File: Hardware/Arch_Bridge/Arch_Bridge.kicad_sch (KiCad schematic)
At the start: 94 parts, among them J1 Conn_01x02, J5V1 Conn_01x02, Q1 MMBT3904, Q2 MMBT3906, Q3 MJE2955, U1 AP63205WU, U11 ESP32-S3-WROOM-1, U12 TXS0102DCT, U13 DRV8231ADDAR, U17 TXS0102DCT, U18 TXS0102DCT, U19 TXS0108EPW, U2 TLV1117LV33DCYR, U20 TXS0108EPW, U3 LM393B, U4 74LVC1G04, U5 74LVC1G02, U6 TLP2770, U7 DRV8231ADDAR

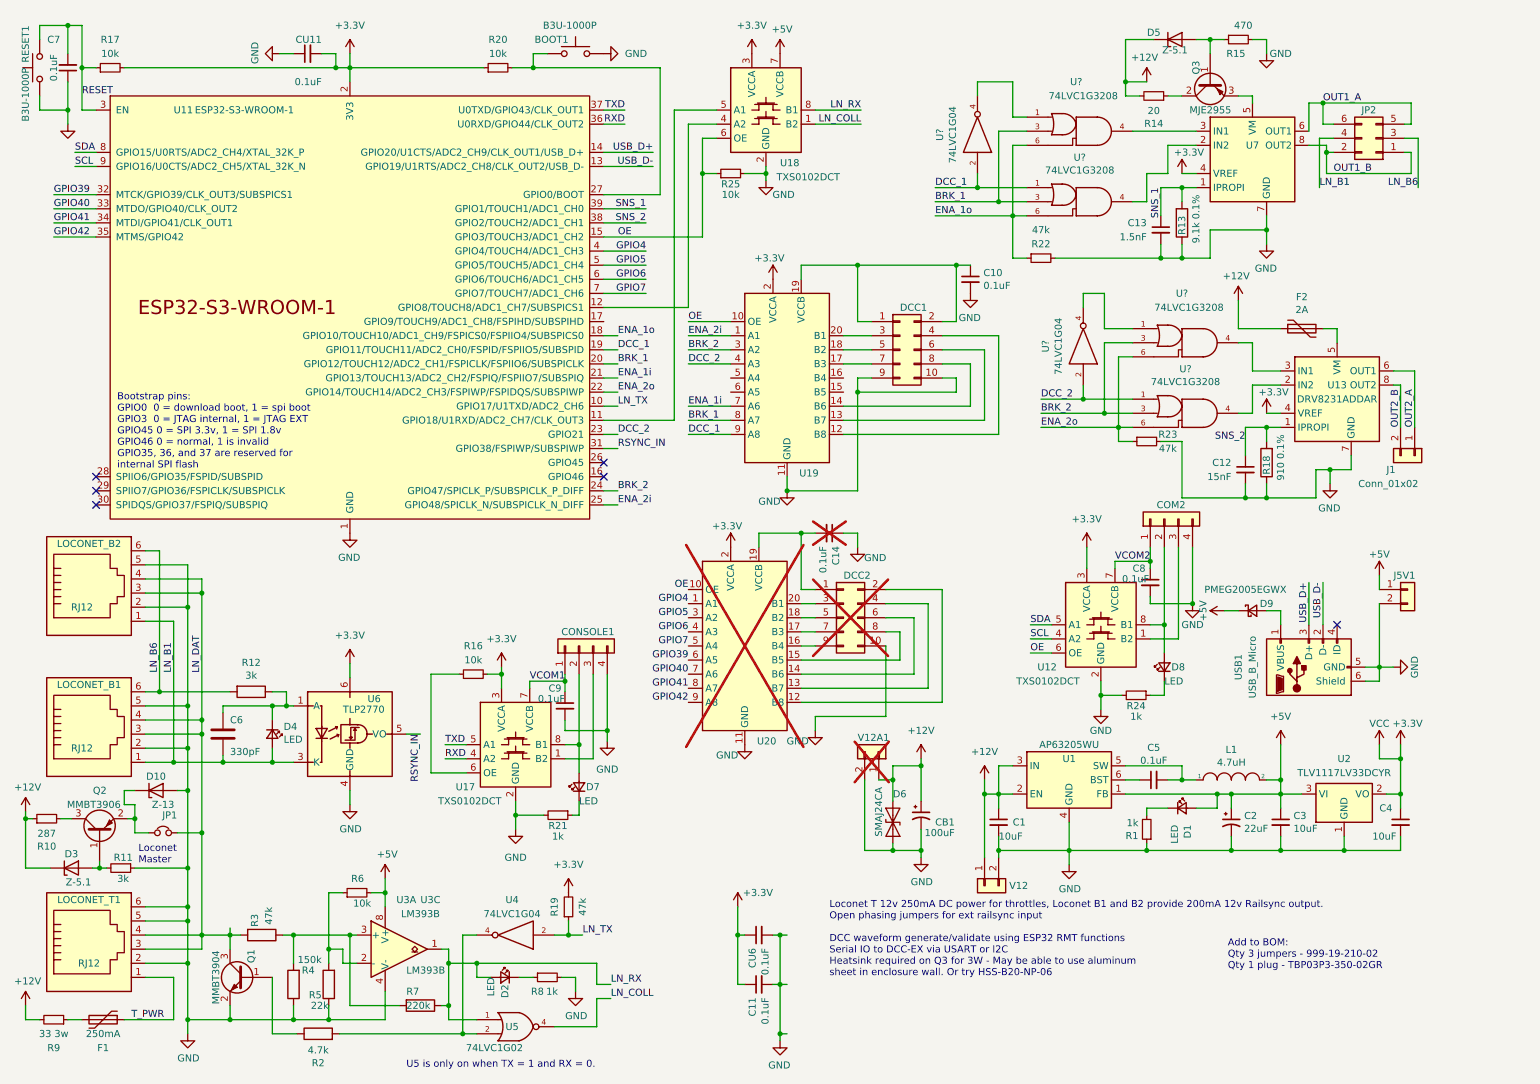
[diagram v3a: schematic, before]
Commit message: Added Railsync voltage monitoring circuit, stabilizer cap. Updated BOM with new parts.
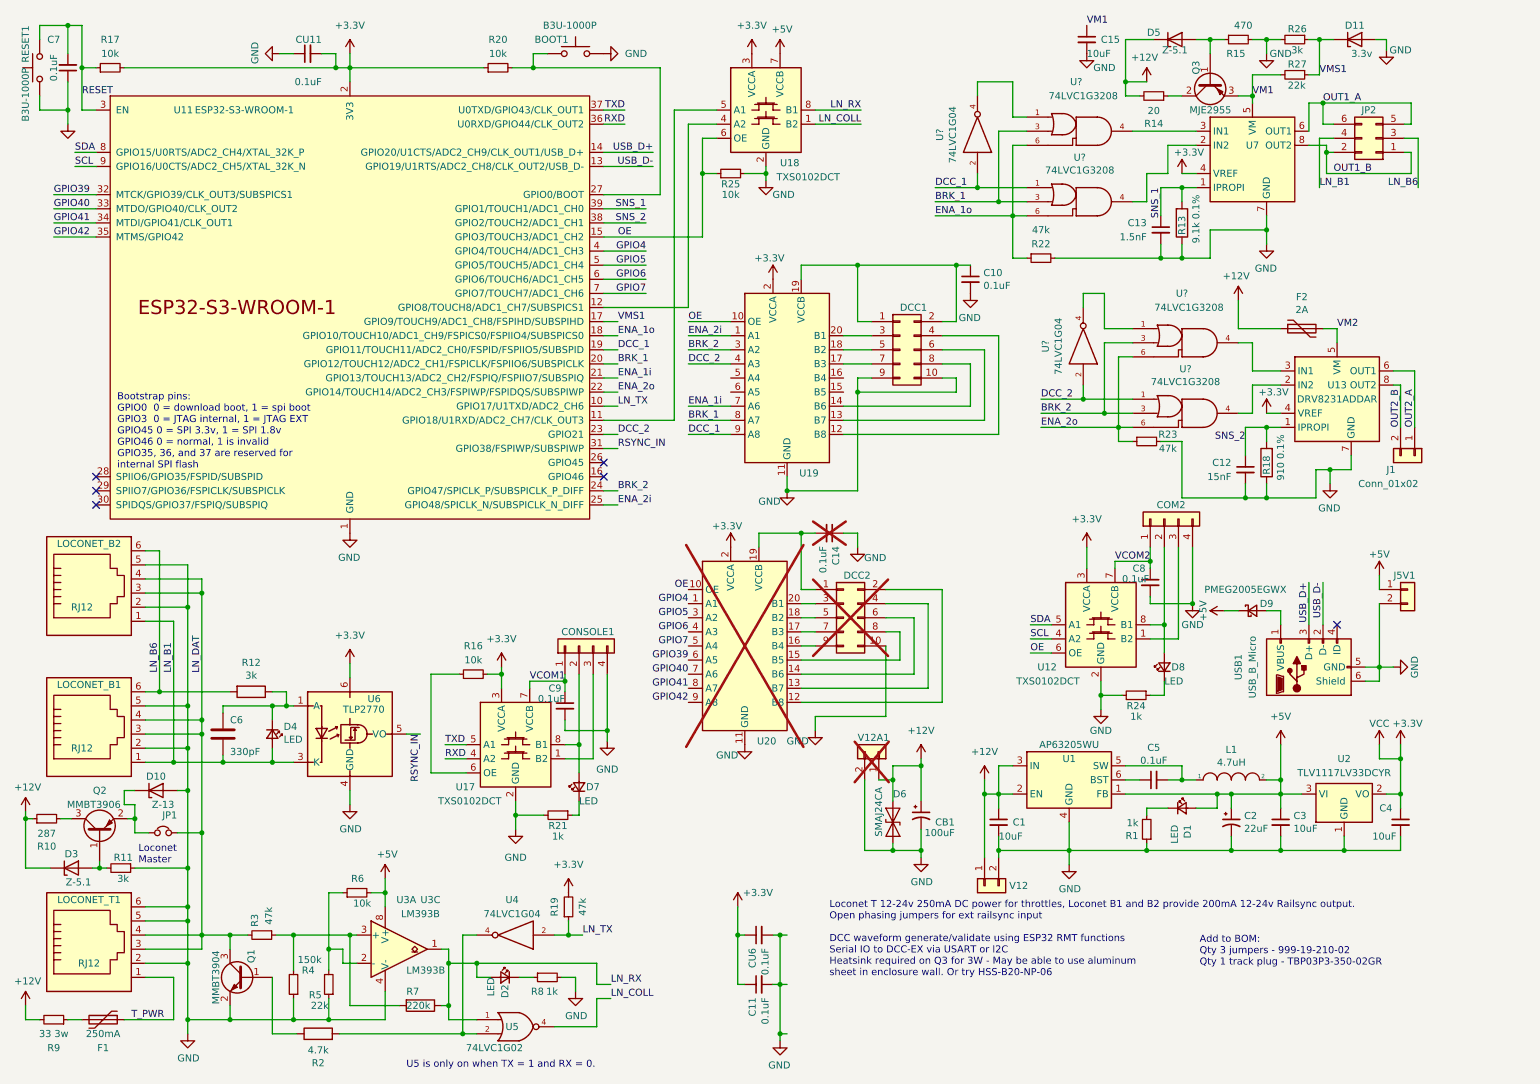
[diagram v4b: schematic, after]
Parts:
- added C15: 10uF, Capacitor_SMD:C_1210_3225Metric, symbol Device:C_Small
- added D11: 3.3v, Diode_SMD:D_MiniMELF, symbol Device:D_Zener
- added R26: 3k, Resistor_SMD:R_1206_3216Metric, symbol Device:R_Small
- added R27: 22k, Resistor_SMD:R_1206_3216Metric, symbol Device:R_Small
- R19: LCSC SKU C4303232 -> C137270
- R3, R4, R5: symbol Device:R -> Device:R_Small
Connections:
- net GND: now also C15.2, D11.2 (A), R26.2
- net VM1: now reaches Q3.3 (E), U7.5 (VM)
- net VM1: now also C15.1, R27.2
- net VMS1: now reaches U11.17 (GPIO9/TOUCH9/ADC1_CH8/FSPIHD/SUBSPIHD)
- net VMS1: now also D11.1 (K), R26.1, R27.1
- net VM2: now reaches F2.2, U13.5 (VM)
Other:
- note added: "Add to BOM: Qty 3 jumpers - 999-19-210-02 Qty 1 track plug - TBP03P3-350-02GR"
- note added: "Loconet T 12-24v 250mA DC power for throttles, Loconet B1 and B2 provide 200mA 12-24v Railsync output. Open phasing jumpers for ext railsync input DCC waveform generate/validate using ESP32 RMT functions Serial IO to DCC-EX via USART or I2C Heatsink required on Q3 for 3W - May be able to use aluminum sheet in enclosure wall. Or try HSS-B20-NP-06"
- note removed: "Add to BOM: Qty 3 jumpers - 999-19-210-02 Qty 1 plug - TBP03P3-350-02GR"
- note removed: "Loconet T 12v 250mA DC power for throttles, Loconet B1 and B2 provide 200mA 12v Railsync output. Open phasing jumpers for ext railsync input DCC waveform generate/validate using ESP32 RMT functions Serial IO to DCC-EX via USART or I2C Heatsink required on Q3 for 3W - May be able to use aluminum sheet in enclosure wall. Or try HSS-B20-NP-06"

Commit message: Replaced TXS0108E with TXB0108 to make use of auto-off feature when ioref is not powered
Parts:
- R22, R23: value 47k -> 150k; LCSC SKU C137270 -> C114931; PN RC1206FR-0747KL -> RC1206FR-07150KL
- U19, U20: value TXS0108EPW -> TXB0108PWR; LCSC SKU C17206 -> C53406; PN TXS0108EPWR -> TXB0108PWR
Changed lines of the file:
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@@
       (effects (font (size 1.27 1.27)))
     )
-    (property "Value" "47k" (at 198.12 52.07 90)
+    (property "Value" "150k" (at 198.12 52.07 90)
       (effects (font (size 1.27 1.27)))
     )
@@
       (effects (font (size 1.27 1.27)) hide)
     )
-    (property "PN" "RC1206FR-0747KL" (at 198.12 57.15 0)
-      (effects (font (size 1.27 1.27)) hide)
-    )
-    (property "LCSC SKU" "C137270" (at 198.12 57.15 0)
+    (property "PN" "RC1206FR-07150KL" (at 198.12 57.15 0)
+      (effects (font (size 1.27 1.27)) hide)
+    )
+    (property "LCSC SKU" "C114931" (at 198.12 57.15 0)
       (effects (font (size 1.27 1.27)) hide)
     )
@@
       (effects (font (size 1.27 1.27)))
     )
-    (property "Value" "47k" (at 220.98 91.44 90)
+    (property "Value" "150k" (at 220.98 91.44 90)
       (effects (font (size 1.27 1.27)))
     )
@@
       (effects (font (size 1.27 1.27)) hide)
     )
-    (property "PN" "RC1206FR-0747KL" (at 217.17 90.17 0)
-      (effects (font (size 1.27 1.27)) hide)
-    )
-    (property "LCSC SKU" "C137270" (at 217.17 90.17 0)
+    (property "PN" "RC1206FR-07150KL" (at 217.17 90.17 0)
+      (effects (font (size 1.27 1.27)) hide)
+    )
+    (property "LCSC SKU" "C114931" (at 217.17 90.17 0)
       (effects (font (size 1.27 1.27)) hide)
     )
@@
       (effects (font (size 1.27 1.27)) (justify left))
     )
-    (property "Value" "TXS0108EPW" (at 146.9741 146.685 0)
+    (property "Value" "TXB0108PWR " (at 146.9741 146.685 0)
       (effects (font (size 1.27 1.27)) (justify left) hide)
     )
@@
       (effects (font (size 1.27 1.27)) hide)
     )
-    (property "Datasheet" "www.ti.com/lit/ds/symlink/txs0108e.pdf" (at 144.78 129.54 0)
+    (property "Datasheet" "https://www.ti.com/lit/gpn/txb0108" (at 144.78 129.54 0)
       (effects (font (size 1.27 1.27)) hide)
     )
@@
       (effects (font (size 1.27 1.27)) hide)
     )
-    (property "PN" "TXS0108EPWR" (at 144.78 127 0)
-      (effects (font (size 1.27 1.27)) hide)
-    )
-    (property "LCSC SKU" "C17206" (at 144.78 127 0)
+    (property "PN" "TXB0108PWR " (at 144.78 127 0)
+      (effects (font (size 1.27 1.27)) hide)
+    )
+    (property "LCSC SKU" "C53406" (at 144.78 127 0)
       (effects (font (size 1.27 1.27)) hide)
     )
@@
       (effects (font (size 1.27 1.27)) (justify left))
     )
-    (property "Value" "TXS0108EPW" (at 154.5941 98.425 0)
+    (property "Value" "TXB0108PWR " (at 154.5941 98.425 0)
       (effects (font (size 1.27 1.27)) (justify left) hide)
     )
@@
       (effects (font (size 1.27 1.27)) hide)
     )
-    (property "Datasheet" "www.ti.com/lit/ds/symlink/txs0108e.pdf" (at 152.4 81.28 0)
+    (property "Datasheet" "https://www.ti.com/lit/gpn/txb0108" (at 152.4 81.28 0)
       (effects (font (size 1.27 1.27)) hide)
     )
@@
       (effects (font (size 1.27 1.27)) hide)
     )
-    (property "PN" "TXS0108EPWR" (at 152.4 78.74 0)
-      (effects (font (size 1.27 1.27)) hide)
-    )
-    (property "LCSC SKU" "C17206" (at 152.4 78.74 0)
-      (effects (font (size 1.27 1.27)) hide)
-    )
+    (property "PN" "TXB0108PWR " (at 152.4 78.74 0)
+      (effects (font (size 1.27 1.27)) hide)
+    )
+    (property "LCSC SKU" "C53406" (at 152.4 78.74 0)
+      (effects (font (size 1.27 1.27)) hide)
+    )

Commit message: Fixed BOM error for JP2, should have been 2x3 pin header not socket.
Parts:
- JP2: footprint Connector_PinSocket_2.54mm:PinSocket_2x03_P2.54mm_Vertical -> Connector_PinHeader_2.54mm:PinHeader_2x03_P2.54mm_Vertical; LCSC SKU C7320823 -> C6360273; MFG Samtec -> Amphenol; PN SSQ-103-01-T-D -> 10129381-906003BLF
- Q2: PN MMBT3906 -> MMBT3906-TP
- U5: value 74LVC1G02 -> 74LVC1G86; symbol Loconet DCC Interface-rescue:74AHCT1G02-74xGxx -> Loconet DCC Interface-rescue:74AHC1G86-74xGxx
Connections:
- net LN_B1: now also JP2.3 (Pin_3); no longer JP2.4 (Pin_4)
- net LN_B6: now also JP2.4 (Pin_4); no longer JP2.3 (Pin_3)
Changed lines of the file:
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@@
     (effects (font (size 1.27 1.27)) (justify right bottom))
   )
-  (label "LN_B6" (at 266.065 44.45 180) (fields_autoplaced)
-    (effects (font (size 1.27 1.27)) (justify right bottom))
+  (label "LN_B6" (at 248.285 44.45 0) (fields_autoplaced)
+    (effects (font (size 1.27 1.27)) (justify left bottom))
   )
   (label "SNS_2" (at 127 50.8 180) (fields_autoplaced)
@@
     (effects (font (size 1.27 1.27)) (justify left bottom))
   )
-  (label "LN_B1" (at 248.285 44.45 0) (fields_autoplaced)
-    (effects (font (size 1.27 1.27)) (justify left bottom))
+  (label "LN_B1" (at 266.065 44.45 180) (fields_autoplaced)
+    (effects (font (size 1.27 1.27)) (justify right bottom))
   )
   (label "BRK_1" (at 134.62 86.36 0) (fields_autoplaced)
@@
       (effects (font (size 1.27 1.27)) hide)
     )
-    (property "Datasheet" "http://www.ti.com/lit/ds/symlink/drv8871.pdf" (at 242.57 38.1 0)
+    (property "Datasheet" "https://www.ti.com/lit/ds/symlink/drv8231a.pdf" (at 242.57 38.1 0)
       (effects (font (size 1.27 1.27)) hide)
     )
@@
     )
   )
-  (symbol (lib_id "Loconet DCC Interface-rescue:74AHCT1G02-74xGxx") (at 104.14 195.58 0) (unit 1)
+  (symbol (lib_id "Loconet DCC Interface-rescue:74AHC1G86-74xGxx") (at 104.14 195.58 0) (unit 1)
     (in_bom yes) (on_board yes) (dnp no)
     (property "Reference" "U5" (at 102.87 195.58 0)
       (effects (font (size 1.27 1.27)))
     )
-    (property "Value" "74LVC1G02" (at 99.695 199.39 0)
+    (property "Value" "74LVC1G86" (at 99.695 199.39 0)
       (effects (font (size 1.27 1.27)))
     )
@@
       (effects (font (size 1.27 1.27)) hide)
     )
-    (property "PN" "MMBT3906" (at 28.575 160.655 0)
+    (property "PN" "MMBT3906-TP" (at 28.575 160.655 0)
       (effects (font (size 1.27 1.27)) hide)
     )
@@
       (effects (font (size 1.27 1.27)) hide)
     )
-    (property "Footprint" "Connector_PinSocket_2.54mm:PinSocket_2x03_P2.54mm_Vertical" (at 258.445 35.56 0)
+    (property "Footprint" "Connector_PinHeader_2.54mm:PinHeader_2x03_P2.54mm_Vertical" (at 258.445 35.56 0)
       (effects (font (size 1.27 1.27)) hide)
     )
@@
       (effects (font (size 1.27 1.27)) hide)
     )
-    (property "LCSC SKU" "C7320823" (at 258.445 35.56 0)
+    (property "LCSC SKU" "C6360273" (at 258.445 35.56 0)
       (effects (font (size 1.27 1.27)) hide)
     )
-    (property "MFG" "Samtec" (at 258.445 35.56 0)
+    (property "MFG" "Amphenol" (at 258.445 35.56 0)
       (effects (font (size 1.27 1.27)) hide)
     )
-    (property "PN" "SSQ-103-01-T-D" (at 258.445 35.56 0)
+    (property "PN" "10129381-906003BLF" (at 258.445 35.56 0)
       (effects (font (size 1.27 1.27)) hide)
     )
@@
       (effects (font (size 1.27 1.27)) hide)
     )
-    (property "Datasheet" "http://www.ti.com/lit/ds/symlink/drv8871.pdf" (at 257.81 81.28 0)
+    (property "Datasheet" "https://www.ti.com/lit/ds/symlink/drv8231a.pdf" (at 257.81 81.28 0)
       (effects (font (size 1.27 1.27)) hide)
     )
